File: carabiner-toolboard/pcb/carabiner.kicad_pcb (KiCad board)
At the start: 2 copper layers, 32.1 x 35.5 mm, 19 parts, among them J1 CommonConnector, J7 CommonConnector

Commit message: Beta 0.1.1 of carabiner
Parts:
- Chamber1: footprint Resistor_SMD:R_0603_1608Metric_Pad1.05x0.95mm_HandSolder -> carabiner-footprints:1206_3216_HandSolder_Hole
- moved Chamber1 0.32 mm to (81.3, 46.5)
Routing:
- net Gnd: track 31.4 -> 28.1 mm
- net DioAux2: track 25.4 -> 26.6 mm
- net ThCom: track 37.5 -> 38.6 mm
- net AltSw: track 37.3 -> 36.4 mm
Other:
- board text added: "Carabiner β0.1.1"
- board text added: "ThCham"
- board text added: "▲ThCham"
- board text removed: "Carabiner β1"
- board text removed: "ThChamb"

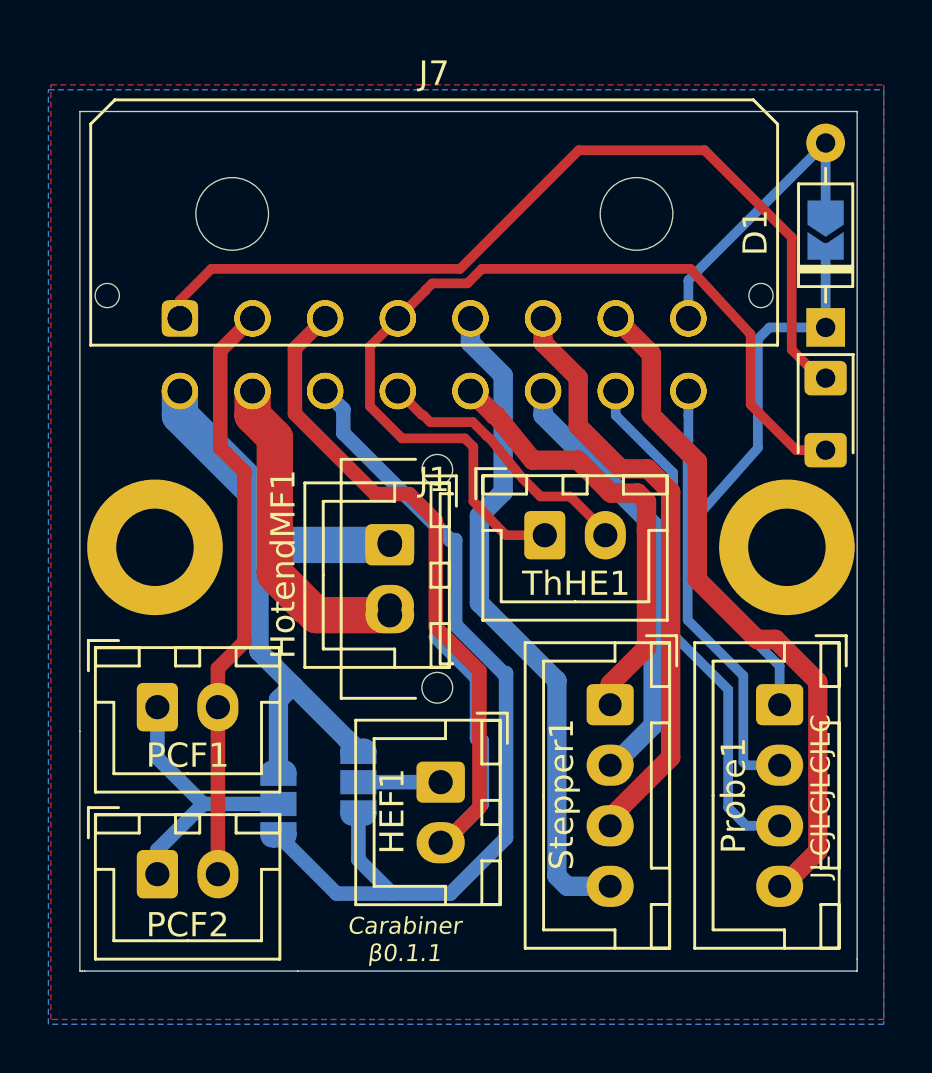
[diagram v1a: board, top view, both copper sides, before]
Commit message: Carabiner Beta 0.2.1 Modified mounting schema (left mounting hole moved down) Modified layout of the connectors Made the horizontal MF compatible with the vertical MF (before mixing them on the 'receiver' and 'sender' would likely cause a short) Improved layout for reduced thermistor interference ChamberThermistor now supported from 0603 up to 1206
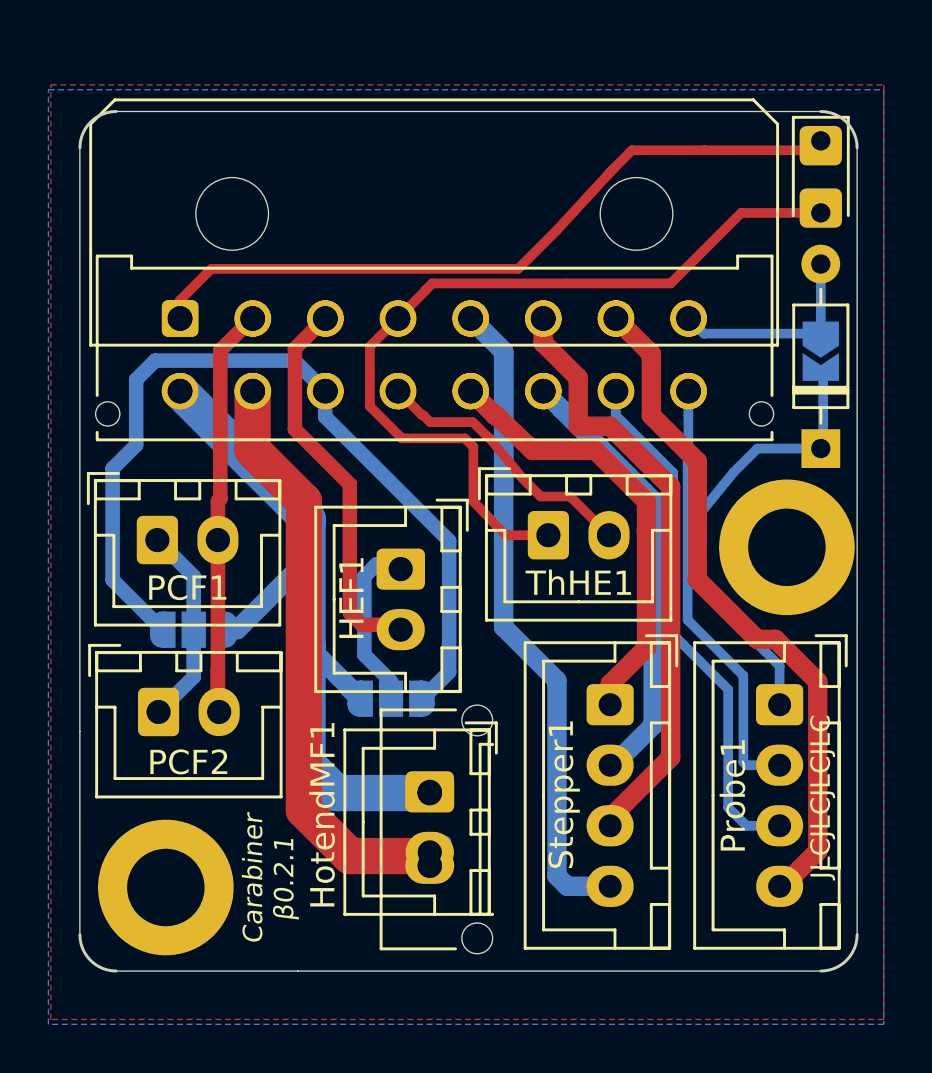
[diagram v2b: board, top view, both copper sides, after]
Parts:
- removed the G*** at (66.4, 37.1)
- removed the G*** at (65.2, 37.1)
- added G***: LOGO, carabiner-footprints:AnnexLogo, B.Cu at (66.0, 37.3)
- added G***: LOGO, carabiner-footprints:AnnexLogo, F.Cu at (66.6, 37.3)
- J1: footprint carabiner-footprints:Molex_Micro-Fit_3.0_2x08_P3.00mm_Vertical -> Connector_Molex:Molex_Micro-Fit_3.0_43045-1612_2x08_P3.00mm_Vertical
- moved H1 14.1 mm to (54.0, 66.0)
- moved HotendMF1 10.5 mm to (65.0, 62.1)
- moved HotendXH1 10.3 mm to (65.0, 62.1)
- moved Chamber1 9.80 mm to (81.1, 36.7)
- moved J1 9.56 mm to (54.6, 42.5)
- moved HEF1 8.95 mm to (63.8, 52.9)
- moved JpPCF1 8.01 mm to (55.2, 55.4), turned to 180 degrees
- moved PCF1 6.90 mm to (53.7, 51.7)
- moved PCF2 6.70 mm to (53.8, 58.8)
- moved D1 5.00 mm to (81.1, 47.9)
- moved JPAux4 5.00 mm to (81.1, 43.9)
- moved JpHEF1 3.70 mm to (63.4, 58.2), turned to 0 degrees
- moved ThHE1 0.15 mm to (69.8, 51.5)
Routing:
- net HotendFanGnd: track 37.0 -> 15.9 mm
- net Common24V: track 40.2 -> 32.4 mm
- net Stepper1A: track 27.8 -> 34.7 mm
- net AltSw: track 36.4 -> 30.0 mm
- net PcFanGnd: track 24.4 -> 18.5 mm
- net DioAux2: track 26.6 -> 21.7 mm
- net ThCom: track 38.6 -> 34.1 mm
- net Aux2: track 14.2 -> 10.3 mm
- net HotendFanSwitch: track 3.40 -> 7.21 mm
- net PcFanSwitch: track 11.6 -> 8.32 mm
- net AltVolt: track 36.9 -> 35.5 mm
- net HotendNeg: track 23.7 -> 24.3 mm
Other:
- outline, holes or cut-outs redrawn
- board text added: "Carabiner β0.2.1"
- board text added: "MotorA"
- board text added: "MotorB"
- board text added: "MotorC"
- board text added: "MotorD"
- board text added: "ThCham ▼"
- board text added: "ThHE"
- board text removed: "Carabiner β0.1.1"
- board text removed: "Motor1"
- board text removed: "Motor2"
- board text removed: "Motor3"
- board text removed: "Motor4"
- board text removed: "ThHot"
- board text removed: "▲ ThHot"
- board text removed: "▲ThCham"

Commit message: Carabiner Beta 0.2.2
[REFACTORING]
Rename nets to be more clear & consistent.
Refactor labels to be have more concise names
Rework traceWidth of the new nets (thinner, still more than enough power)

[FEATURE]
Split up 3-pronged jumper voltage jumper into 2 seperate ones.
Add support for new connectors:
Support 43045 1621 for the commonConnector
Support 43045 0212 for the hotendConnector
Support 43645 0215 for the thermistor
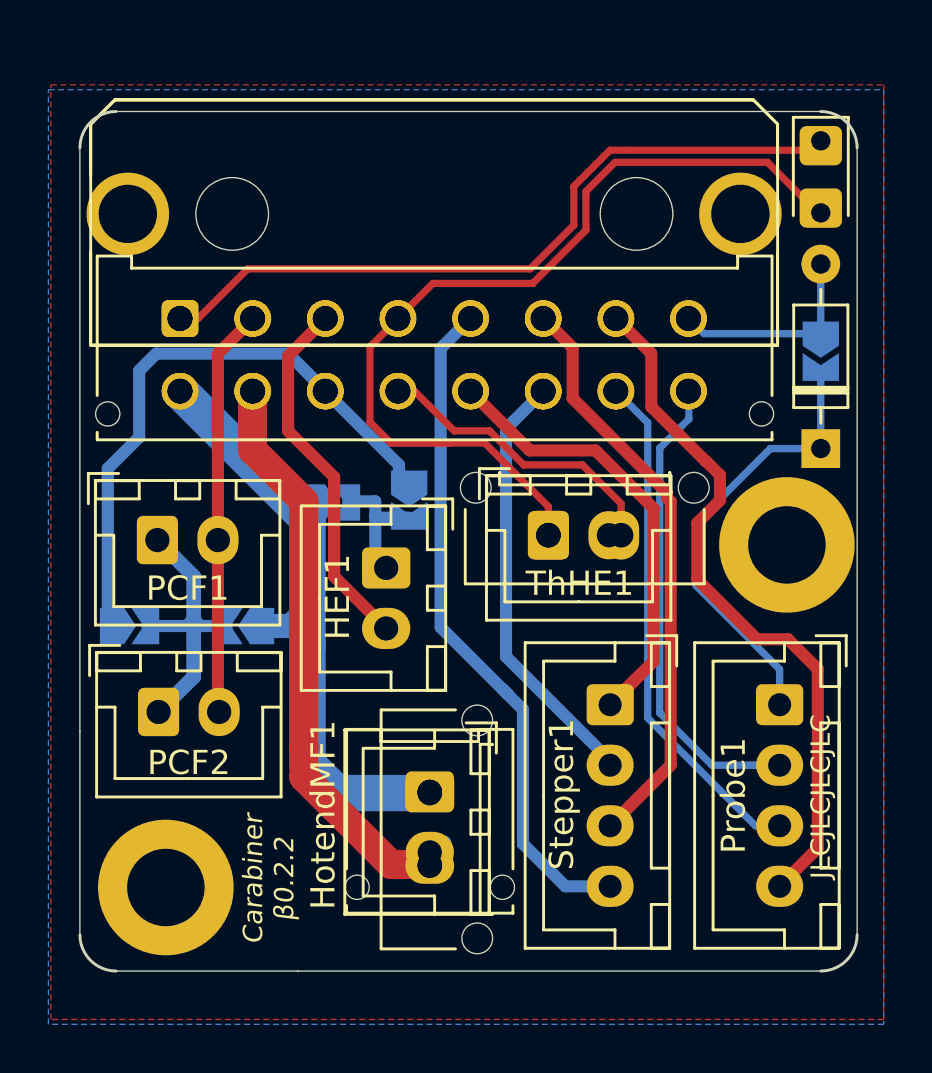
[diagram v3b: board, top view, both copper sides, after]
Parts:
- removed G*** (x2): LOGO, carabiner-footprints:AnnexLogo
- removed JpHEF1, JpPCF1: SolderJumper_3_Open-Jumper, Jumper:SolderJumper-3_P1.3mm_Open_RoundedPad1.0x1.5mm_NumberLabels
- added HEF_A: SolderJumper_2_Open, Jumper:SolderJumper-2_P1.3mm_Open_TrianglePad1.0x1.5mm, B.Cu at (64.1, 50.0)
- added HEF_M: SolderJumper_2_Open, Jumper:SolderJumper-2_P1.3mm_Open_TrianglePad1.0x1.5mm, B.Cu at (60.9, 50.1)
- added HotendMF2: Hotend MF 43045-0212, Connector_Molex:Molex_Micro-Fit_3.0_43045-0212_2x01_P3.00mm_Vertical, F.Cu at (65.0, 62.1)
- added J2: MF-Horizontal 43045-1621, Connector_Molex:Molex_Micro-Fit_3.0_43045-1621_2x08-1MP_P3.00mm_Horizontal, F.Cu at (54.6, 42.5)
- added LOGO1: Logo_Open_Hardware_Small, Annex:AnnexLogo, F.Cu at (65.4, 37.3)
- added LOGO2: Logo_Open_Hardware_Small, Annex:AnnexLogoBack, F.Cu at (66.7, 37.3)
- added PCF_A: SolderJumper_2_Open, Jumper:SolderJumper-2_P1.3mm_Open_TrianglePad1.0x1.5mm, B.Cu at (52.5, 55.2)
- added PCF_M: SolderJumper_2_Open, Jumper:SolderJumper-2_P1.3mm_Open_TrianglePad1.0x1.5mm, B.Cu at (57.3, 55.2)
- added ThHe_MF1: Thermistor MF 43650-0215, Connector_Molex:Molex_Micro-Fit_3.0_43650-0215_1x02_P3.00mm_Vertical, F.Cu at (69.8, 51.5)
- HotendMF1: value HotendTool -> Hotend MF 43650-0215
- J1: value CommonConnector -> MF-Vertical 43045-1612
- J7: value CommonConnector -> MF-Horizontal 43045-1600
- moved HEF1 0.60 mm to (63.1, 52.9)
- moved H2 0.10 mm to (79.7, 51.9)
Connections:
- net AltSw renamed ThChamber
- net Common24V renamed HotendVoltage
- net ThCom renamed ThCommonGnd
- net ThHot renamed ThHotend
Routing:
- net AltVolt: track 35.5 -> 24.7 mm
- net Stepper1A: track 34.7 -> 28.4 mm
- net HotendVoltage: track 32.4 -> 26.8 mm
- net ThCommonGnd: track 34.1 -> 37.7 mm
- net PcFanSwitch: track 8.32 -> 11.9 mm
- net Aux1: track 18.2 -> 21.6 mm
- net DioAux2: track 21.7 -> 18.7 mm
- net Stepper1B: track 24.9 -> 27.8 mm
- net Stepper2B: track 18.3 -> 20.2 mm
- net Aux2: track 10.3 -> 8.58 mm
- net PcFanGnd: track 18.5 -> 16.9 mm
- net ThHotend: track 12.2 -> 13.6 mm
- net Gnd: track 28.1 -> 29.1 mm
- net HotendFanGnd: track 15.9 -> 15.1 mm
- net HotendFanSwitch: track 7.21 -> 6.51 mm
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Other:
- net class 2 Amp added: clearance 0.2, trace_width 0.3, via_dia 0.8, via_drill 0.4
- net class 3 Amp added: clearance 0.2, trace_width 0.5, via_dia 0.8, via_drill 0.4
- net class 4.5 Amp added: clearance 0.2, trace_width 1.2, via_dia 0.8, via_drill 0.4
- board text added: "Carabiner β0.2.2"
- board text added: "HeVolt"
- board text added: "◀ ThChamb"
- board text removed: "Carabiner β0.2.1"
- board text removed: "ThCham ▼"

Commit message: Carabiner Beta 0.2.3
Fix traces being too small (too little amperage supported)
Update README
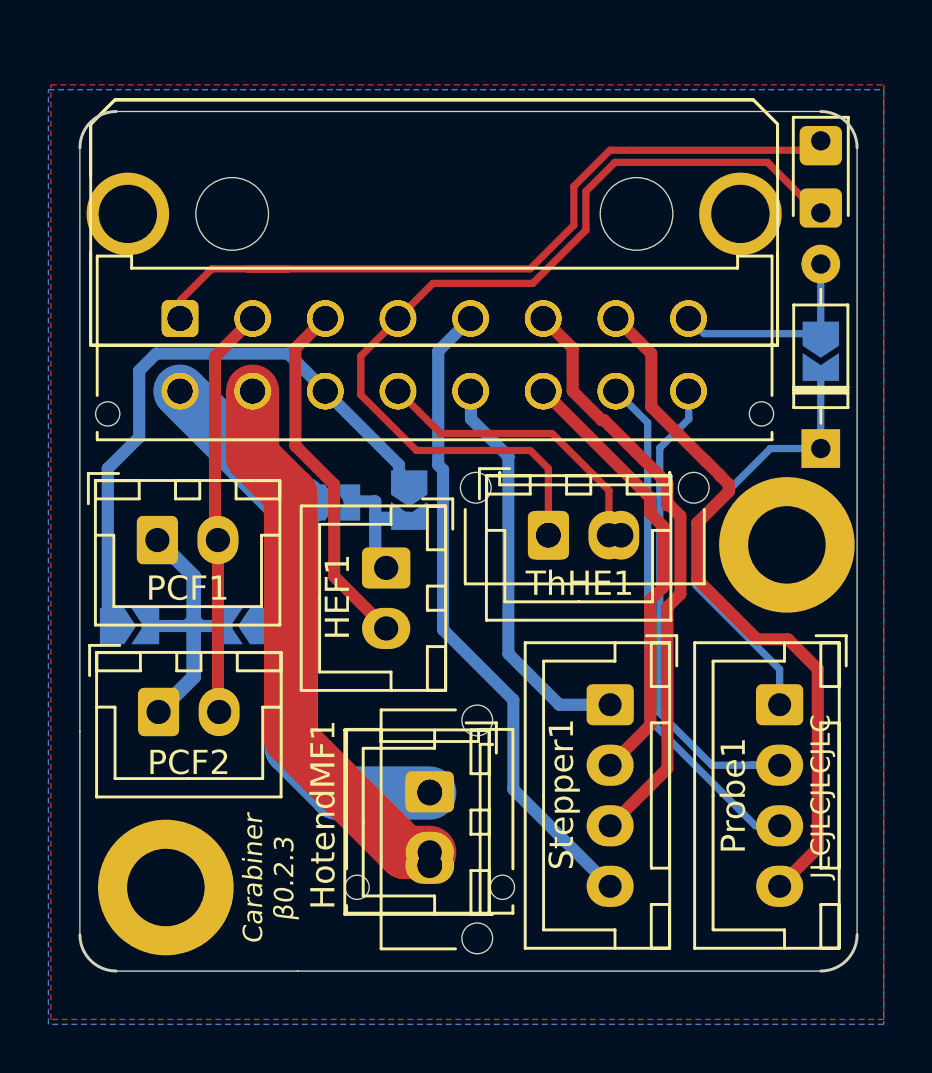
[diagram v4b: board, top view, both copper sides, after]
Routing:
- net Stepper2B: track 20.2 -> 16.6 mm
- net Stepper1B: track 27.8 -> 24.9 mm
- net HotendVoltage: track 26.8 -> 24.7 mm
- net ThChamber: track 30.7 -> 32.8 mm
- net Stepper1A: track 28.4 -> 27.1 mm
- net ThCommonGnd: track 37.7 -> 38.6 mm
- net Stepper2A: track 18.0 -> 18.9 mm
- net HotendNeg: track 23.7 -> 22.8 mm
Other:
- net class 4.5 Amp: trace_width 1.2 -> 2
- board text added: "Carabiner β0.2.3"
- board text removed: "Carabiner β0.2.2"

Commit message: Carabiner R1 - 'Unlimited Power'
Increase maximum hotend amperage (100W heaters are now supported!)
Minor silkscreen adaptions
Add folders for attachments & variants
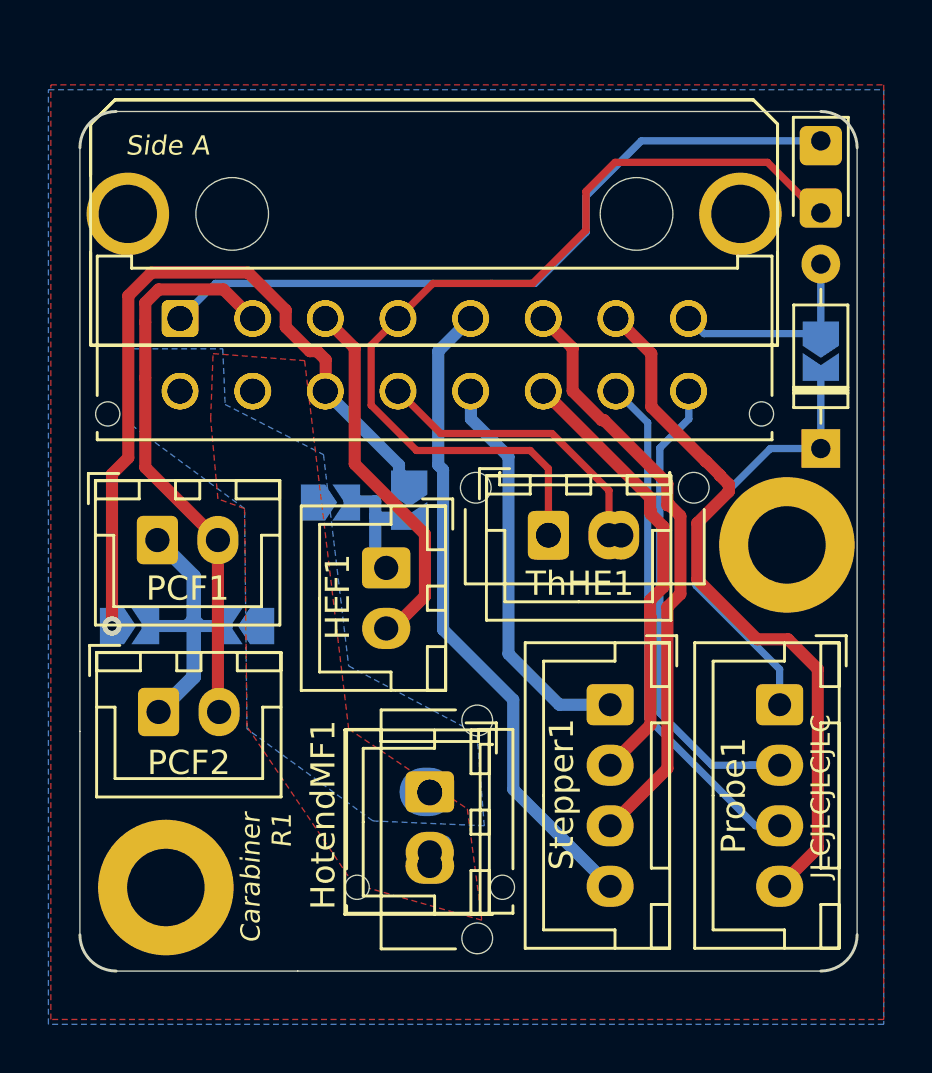
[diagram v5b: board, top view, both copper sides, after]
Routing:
- net HotendVoltage: track 24.7 -> 0.25 mm
- net HotendNeg: track 22.8 -> 0.15 mm
- net PcFanGnd: track 17.0 -> 23.3 mm
- net AltVolt: track 24.7 -> 30.9 mm, vias 0 -> 1
- net ThChamber: track 32.8 -> 31.2 mm
- added copper zone on F.Cu, net HotendNeg
- added copper zone on B.Cu, net HotendVoltage
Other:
- net class 2 Amp removed
- net class 3 Amp removed
- net class 4.5 Amp removed
- net class Default removed
- net class FanAmp removed
- net class HighAmp removed
- net class LowAmp removed
- net class MediumAmp removed
- board text added: "Carabiner R1"
- board text added: "Side A"
- board text added: "Side B"
- board text removed: "Carabiner β0.2.3"
